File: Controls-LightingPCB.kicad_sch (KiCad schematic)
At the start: 92 parts, among them J1 MinionConn, J10 INTERNAL_RIGHTBLINK, J11 INTERNAL_LEFTBLINK, J12 EXTERNAL_RIGHTBLINK, J13 EXTERNAL_HDLT, J14 EXTERNAL_BRAKELIGHT, J2 12VPWRCONN, J3 CRUZ_ST_INDICATOR_33v, J4 CRUZ_EN_INDICATOR_33v, J5 REGEN_INDICATOR_33v, J6 NEU_INDICATOR_33v, J7 FOR_INDICATOR_33v, J8 REV_INDICATOR_33v, J9 EXTERNAL_LEFTBLINK, Q1 2N7000, Q2 2N7000, Q3 2N7000, Q4 2N7000, Q5 2N7000, SW1 CRUISE_SET, SW2 CRUISE_ENABLE, SW3 F/R_SW, SW4 REGEN_SW, SW5 TURN_SIGNAL_SW, U1 NCP1117-3.3_SOT223

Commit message: Pico-Claps connectors + traces
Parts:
- HZD_SW1, J10, J11, J12, J13, J14, J2, J3, J4, J5, J6, J7, J8, J9, SW1, SW2, SW4: footprint Connector_Molex:Molex_Micro-Fit_3.0_43650-0200_1x02_P3.00mm_Horizontal -> Connector_Molex:Molex_Pico-Clasp_501331-0207_1x02-1MP_P1.00mm_Vertical
- J1: footprint Connector_Molex:Molex_Micro-Fit_3.0_43650-0900_1x09_P3.00mm_Horizontal -> Connector_Molex:Molex_Pico-Clasp_501331-0907_1x09-1MP_P1.00mm_Vertical
- SW3, SW5: footprint Connector_Molex:Molex_Micro-Fit_3.0_43650-0300_1x03_P3.00mm_Horizontal -> Connector_Molex:Molex_Pico-Clasp_501331-0307_1x03-1MP_P1.00mm_Vertical

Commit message: Changed to SMD mosfets
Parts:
- Q1, Q2, Q3, Q4, Q5: footprint Package_TO_SOT_THT:TO-92_Inline -> Package_TO_SOT_SMD:SOT-23
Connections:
- net +3V3 renamed +3.3V
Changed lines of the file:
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@@
     (property "Reference" "Q3" (id 0) (at 237.49 93.98 90))
     (property "Value" "2N7000" (id 1) (at 237.49 96.52 90))
-    (property "Footprint" "Package_TO_SOT_THT:TO-92_Inline" (id 2) (at 235.585 97.79 0)
+    (property "Footprint" "Package_TO_SOT_SMD:SOT-23" (id 2) (at 235.585 97.79 0)
       (effects (font (size 1.27 1.27) italic) (justify left) hide)
     )
-    (property "Datasheet" "https://www.vishay.com/docs/70226/70226.pdf" (id 3) (at 237.49 102.87 0)
+    (property "Datasheet" "https://www.mouser.com/datasheet/2/916/2N7002H-2909812.pdf" (id 3) (at 237.49 102.87 0)
       (effects (font (size 1.27 1.27)) (justify left) hide)
     )
@@
     (property "Reference" "Q5" (id 0) (at 238.76 21.59 90))
     (property "Value" "2N7000" (id 1) (at 238.76 24.13 90))
-    (property "Footprint" "Package_TO_SOT_THT:TO-92_Inline" (id 2) (at 236.855 25.4 0)
+    (property "Footprint" "Package_TO_SOT_SMD:SOT-23" (id 2) (at 236.855 25.4 0)
       (effects (font (size 1.27 1.27) italic) (justify left) hide)
     )
-    (property "Datasheet" "https://www.vishay.com/docs/70226/70226.pdf" (id 3) (at 238.76 30.48 0)
+    (property "Datasheet" "https://www.mouser.com/datasheet/2/916/2N7002H-2909812.pdf" (id 3) (at 238.76 30.48 0)
       (effects (font (size 1.27 1.27)) (justify left) hide)
     )
@@
     (property "Reference" "Q2" (id 0) (at 237.49 69.85 90))
     (property "Value" "2N7000" (id 1) (at 237.49 72.39 90))
-    (property "Footprint" "Package_TO_SOT_THT:TO-92_Inline" (id 2) (at 235.585 73.66 0)
+    (property "Footprint" "Package_TO_SOT_SMD:SOT-23" (id 2) (at 235.585 73.66 0)
       (effects (font (size 1.27 1.27) italic) (justify left) hide)
     )
-    (property "Datasheet" "https://www.vishay.com/docs/70226/70226.pdf" (id 3) (at 237.49 78.74 0)
+    (property "Datasheet" "https://www.mouser.com/datasheet/2/916/2N7002H-2909812.pdf" (id 3) (at 237.49 78.74 0)
       (effects (font (size 1.27 1.27)) (justify left) hide)
     )
@@
     (property "Reference" "Q1" (id 0) (at 237.49 45.72 90))
     (property "Value" "2N7000" (id 1) (at 237.49 48.26 90))
-    (property "Footprint" "Package_TO_SOT_THT:TO-92_Inline" (id 2) (at 235.585 49.53 0)
+    (property "Footprint" "Package_TO_SOT_SMD:SOT-23" (id 2) (at 235.585 49.53 0)
       (effects (font (size 1.27 1.27) italic) (justify left) hide)
     )
-    (property "Datasheet" "https://www.vishay.com/docs/70226/70226.pdf" (id 3) (at 237.49 54.61 0)
+    (property "Datasheet" "https://www.mouser.com/datasheet/2/916/2N7002H-2909812.pdf" (id 3) (at 237.49 54.61 0)
       (effects (font (size 1.27 1.27)) (justify left) hide)
     )
@@
     (property "Reference" "Q4" (id 0) (at 247.015 150.495 0))
     (property "Value" "2N7000" (id 1) (at 247.015 153.035 0))
-    (property "Footprint" "Package_TO_SOT_THT:TO-92_Inline" (id 2) (at 243.205 153.67 0)
+    (property "Footprint" "Package_TO_SOT_SMD:SOT-23" (id 2) (at 243.205 153.67 0)
       (effects (font (size 1.27 1.27) italic) (justify left) hide)
     )
-    (property "Datasheet" "https://www.vishay.com/docs/70226/70226.pdf" (id 3) (at 238.125 151.765 0)
+    (property "Datasheet" "https://www.mouser.com/datasheet/2/916/2N7002H-2909812.pdf" (id 3) (at 238.125 151.765 0)
       (effects (font (size 1.27 1.27)) (justify left) hide)
     )
@@
     )
     (path "/ad0e8c56-9523-4294-a2ce-615be15ed23f"
-      (reference "Q1") (unit 1) (value "2N7000") (footprint "Package_TO_SOT_THT:TO-92_Inline")
+      (reference "Q1") (unit 1) (value "2N7000") (footprint "Package_TO_SOT_SMD:SOT-23")
     )
     (path "/a5dd49cb-a130-4999-9533-e26323d7662d"
-      (reference "Q2") (unit 1) (value "2N7000") (footprint "Package_TO_SOT_THT:TO-92_Inline")
+      (reference "Q2") (unit 1) (value "2N7000") (footprint "Package_TO_SOT_SMD:SOT-23")
     )
     (path "/3198a27d-6bfc-45eb-bfb7-7dcd7e675f29"
-      (reference "Q3") (unit 1) (value "2N7000") (footprint "Package_TO_SOT_THT:TO-92_Inline")
+      (reference "Q3") (unit 1) (value "2N7000") (footprint "Package_TO_SOT_SMD:SOT-23")
     )
     (path "/cf06b1f1-2a1d-4ba2-bbf7-922b9eaa6d79"
-      (reference "Q4") (unit 1) (value "2N7000") (footprint "Package_TO_SOT_THT:TO-92_Inline")
+      (reference "Q4") (unit 1) (value "2N7000") (footprint "Package_TO_SOT_SMD:SOT-23")
     )
     (path "/8c4da0ba-68dc-4ea9-bd3d-de81e85c559f"
-      (reference "Q5") (unit 1) (value "2N7000") (footprint "Package_TO_SOT_THT:TO-92_Inline")
+      (reference "Q5") (unit 1) (value "2N7000") (footprint "Package_TO_SOT_SMD:SOT-23")
     )
     (path "/bf79cd79-9bbf-496d-a03d-63973600490a"

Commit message: First bad layout
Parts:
- HZD_SW1, J10, J11, J12, J13, J14, J2, J3, J4, J5, J6, J7, J8, J9, SW1, SW2, SW4: footprint Connector_Molex:Molex_Pico-Clasp_501331-0207_1x02-1MP_P1.00mm_Vertical -> Connector_Molex:Molex_Micro-Fit_3.0_43650-0215_1x02_P3.00mm_Vertical
- J1: footprint Connector_Molex:Molex_Pico-Clasp_501331-0907_1x09-1MP_P1.00mm_Vertical -> Connector_Molex:Molex_Micro-Fit_3.0_43650-0900_1x09_P3.00mm_Horizontal
- SW3, SW5: footprint Connector_Molex:Molex_Pico-Clasp_501331-0307_1x03-1MP_P1.00mm_Vertical -> Connector_Molex:Molex_Micro-Fit_3.0_43650-0315_1x03_P3.00mm_Vertical

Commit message: finished layout
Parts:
- removed R18, R19: 100k, Resistor_SMD:R_0805_2012Metric, symbol Device:R_Small
- CRUZ EN IND1: renamed from J4
- CRUZ EN SW1: renamed from SW2
- CRUZ SET IND1: renamed from J3
- CRUZ SET SW1: renamed from SW1
- F/R SW1: renamed from SW3; footprint Connector_Molex:Molex_Micro-Fit_3.0_43650-0315_1x03_P3.00mm_Vertical -> Connector_Molex:Molex_Micro-Fit_3.0_43650-0415_1x04_P3.00mm_Vertical
- FORWARD IND1: renamed from J7
- HZD SW1: renamed from HZD_SW1
- L BLINK EXT1: renamed from J9
- L BLINK INT1: renamed from J11
- NEUTRAL IND1: renamed from J6
- R BLINK EXT1: renamed from J12
- R BLINK INT1: renamed from J10
- REGEN IND1: renamed from J5
- REGEN SW1: renamed from SW4
- REV IND1: renamed from J8
- Turn Signal SW1: renamed from SW5
- renumbered TP5 to 12V1, TP3 to 3V3, TP6 to 5V1, J14 to BRAKELIGHT1, TP9 to CLK1, TP2 to GND1, TP1 to GNDPWR1, J13 to HEADLIGHT2, TP8 to Headlight1, TP4 to LeftBlink1, J2 to PWR1, TP7 to RightBlink1

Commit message: component updates
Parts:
- C9: value 10uF -> 33 uF
- R10, R13, R14, R15, R4, R5: value 0k -> 100 Ohm
- R20, R21: value 0k -> 0 Ohm
- R23, R24: value 0 Ohm -> 500 Ohm
- R8: value 6.8k -> 10k
- R9: value 56k -> 10k
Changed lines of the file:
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@@
     (in_bom yes) (on_board yes)
     (property "Reference" "R13" (id 0) (at 172.085 120.015 0))
-    (property "Value" "0k" (id 1) (at 172.085 121.92 0))
+    (property "Value" "100 Ohm" (id 1) (at 173.99 121.92 0))
     (property "Footprint" "Resistor_SMD:R_0805_2012Metric" (id 2) (at 168.91 119.38 0)
       (effects (font (size 1.27 1.27)) hide)
@@
     (in_bom yes) (on_board yes)
     (property "Reference" "R20" (id 0) (at 232.41 120.015 90))
-    (property "Value" "0k" (id 1) (at 232.41 122.555 90))
+    (property "Value" "0 Ohm" (id 1) (at 232.41 122.555 90))
     (property "Footprint" "Resistor_SMD:R_0805_2012Metric" (id 2) (at 230.505 127 0)
       (effects (font (size 1.27 1.27)) hide)
@@
     (in_bom yes) (on_board yes)
     (property "Reference" "R24" (id 0) (at 238.76 86.36 90))
-    (property "Value" "0 Ohm" (id 1) (at 240.03 88.9 90))
+    (property "Value" "500 Ohm" (id 1) (at 240.03 88.9 90))
     (property "Footprint" "Resistor_SMD:R_0805_2012Metric" (id 2) (at 237.49 91.44 0)
       (effects (font (size 1.27 1.27)) hide)
@@
     (in_bom yes) (on_board yes)
     (property "Reference" "R14" (id 0) (at 173.355 132.715 0))
-    (property "Value" "0k" (id 1) (at 173.355 134.62 0))
+    (property "Value" "100 Ohm" (id 1) (at 176.53 134.62 0))
     (property "Footprint" "Resistor_SMD:R_0805_2012Metric" (id 2) (at 170.815 132.715 0)
       (effects (font (size 1.27 1.27)) hide)
@@
       (effects (font (size 1.27 1.27)) (justify right))
     )
-    (property "Value" "56k" (id 1) (at 135.89 55.8799 0)
+    (property "Value" "10k" (id 1) (at 135.89 55.8799 0)
       (effects (font (size 1.27 1.27)) (justify right))
     )
@@
     (in_bom yes) (on_board yes)
     (property "Reference" "R21" (id 0) (at 233.045 137.16 90))
-    (property "Value" "0k" (id 1) (at 233.045 139.7 90))
+    (property "Value" "0 Ohm" (id 1) (at 233.045 139.7 90))
     (property "Footprint" "Resistor_SMD:R_0805_2012Metric" (id 2) (at 231.14 144.145 0)
       (effects (font (size 1.27 1.27)) hide)
@@
       (effects (font (size 1.27 1.27)) (justify left))
     )
-    (property "Value" "6.8k" (id 1) (at 135.89 48.2599 0)
+    (property "Value" "10k" (id 1) (at 135.89 48.2599 0)
       (effects (font (size 1.27 1.27)) (justify left))
     )
@@
     (in_bom yes) (on_board yes)
     (property "Reference" "R15" (id 0) (at 177.165 144.78 0))
-    (property "Value" "0k" (id 1) (at 177.165 146.685 0))
+    (property "Value" "100 Ohm" (id 1) (at 179.07 147.32 0))
     (property "Footprint" "Resistor_SMD:R_0805_2012Metric" (id 2) (at 173.99 144.145 0)
       (effects (font (size 1.27 1.27)) hide)
@@
     (in_bom yes) (on_board yes)
     (property "Reference" "R10" (id 0) (at 139.7 115.57 90))
-    (property "Value" "0k" (id 1) (at 139.7 117.475 90))
+    (property "Value" "100 Ohm" (id 1) (at 140.97 116.84 90))
     (property "Footprint" "Resistor_SMD:R_0805_2012Metric" (id 2) (at 137.795 112.395 0)
       (effects (font (size 1.27 1.27)) hide)
@@
     (in_bom yes) (on_board yes)
     (property "Reference" "R4" (id 0) (at 81.28 117.475 90))
-    (property "Value" "0k" (id 1) (at 81.28 119.38 90))
+    (property "Value" "100 Ohm" (id 1) (at 83.82 119.38 90))
     (property "Footprint" "Resistor_SMD:R_0805_2012Metric" (id 2) (at 79.375 114.3 0)
       (effects (font (size 1.27 1.27)) hide)
@@
       (effects (font (size 1.27 1.27)) (justify left))
     )
-    (property "Value" "10uF" (id 1) (at 127 63.5 0)
+    (property "Value" "33 uF" (id 1) (at 127 63.5 0)
       (effects (font (size 1.27 1.27)) (justify left))
     )
@@
     (in_bom yes) (on_board yes)
     (property "Reference" "R5" (id 0) (at 81.915 156.21 90))
-    (property "Value" "0k" (id 1) (at 81.915 158.115 90))
+    (property "Value" "100 Ohm" (id 1) (at 83.82 158.75 90))
     (property "Footprint" "Resistor_SMD:R_0805_2012Metric" (id 2) (at 80.01 153.035 0)
       (effects (font (size 1.27 1.27)) hide)
@@
     (in_bom yes) (on_board yes)
     (property "Reference" "R23" (id 0) (at 238.76 62.23 90))
-    (property "Value" "0 Ohm" (id 1) (at 240.03 64.77 90))
+    (property "Value" "500 Ohm" (id 1) (at 240.03 64.77 90))
     (property "Footprint" "Resistor_SMD:R_0805_2012Metric" (id 2) (at 237.49 67.31 0)
       (effects (font (size 1.27 1.27)) hide)
@@
     )
     (path "/b3a55782-cbfa-4ad7-a3bc-1a21e5b9d7e1"
-      (reference "C9") (unit 1) (value "10uF") (footprint "Capacitor_SMD:C_0805_2012Metric")
+      (reference "C9") (unit 1) (value "33 uF") (footprint "Capacitor_SMD:C_0805_2012Metric")
     )
     (path "/03b27535-447c-483c-8e98-454a6a39168a"
@@
     )
     (path "/9c10fc17-ccfe-4e69-aa86-c672041d3ca2"
-      (reference "R4") (unit 1) (value "0k") (footprint "Resistor_SMD:R_0805_2012Metric")
+      (reference "R4") (unit 1) (value "100 Ohm") (footprint "Resistor_SMD:R_0805_2012Metric")
     )
     (path "/bf67ec5a-fdc9-4655-ae9a-dfe5faf72199"
-      (reference "R5") (unit 1) (value "0k") (footprint "Resistor_SMD:R_0805_2012Metric")
+      (reference "R5") (unit 1) (value "100 Ohm") (footprint "Resistor_SMD:R_0805_2012Metric")
     )
     (path "/0b46dd1c-57a4-4d34-a081-aa58b25354f8"
@@
     )
     (path "/579a53c9-ab3c-4032-a13e-83c57f96dbc9"
-      (reference "R8") (unit 1) (value "6.8k") (footprint "Resistor_SMD:R_0805_2012Metric")
+      (reference "R8") (unit 1) (value "10k") (footprint "Resistor_SMD:R_0805_2012Metric")
     )
     (path "/35b071f2-161c-49bc-b89a-f680527e0dea"
-      (reference "R9") (unit 1) (value "56k") (footprint "Resistor_SMD:R_0805_2012Metric")
+      (reference "R9") (unit 1) (value "10k") (footprint "Resistor_SMD:R_0805_2012Metric")
     )
     (path "/943566fc-e0ec-4811-a35c-3b8867aae60d"
-      (reference "R10") (unit 1) (value "0k") (footprint "Resistor_SMD:R_0805_2012Metric")
+      (reference "R10") (unit 1) (value "100 Ohm") (footprint "Resistor_SMD:R_0805_2012Metric")
     )
     (path "/421bd5df-1649-4123-ab2b-fa7f213c86e8"
@@
     )
     (path "/08e7c18d-e700-4c5b-ae98-5a65f509b387"
-      (reference "R13") (unit 1) (value "0k") (footprint "Resistor_SMD:R_0805_2012Metric")
+      (reference "R13") (unit 1) (value "100 Ohm") (footprint "Resistor_SMD:R_0805_2012Metric")
     )
     (path "/289f6036-ef79-4e79-8863-68c618e8eafc"
-      (reference "R14") (unit 1) (value "0k") (footprint "Resistor_SMD:R_0805_2012Metric")
+      (reference "R14") (unit 1) (value "100 Ohm") (footprint "Resistor_SMD:R_0805_2012Metric")
     )
     (path "/610c1617-a221-4760-8695-07d2d71b427f"
-      (reference "R15") (unit 1) (value "0k") (footprint "Resistor_SMD:R_0805_2012Metric")
+      (reference "R15") (unit 1) (value "100 Ohm") (footprint "Resistor_SMD:R_0805_2012Metric")
     )
     (path "/5884bc66-6373-4b10-8c5d-8d80d29d8235"
@@
     )
     (path "/0f8225d3-8219-489b-b209-40bdef973e35"
-      (reference "R20") (unit 1) (value "0k") (footprint "Resistor_SMD:R_0805_2012Metric")
+      (reference "R20") (unit 1) (value "0 Ohm") (footprint "Resistor_SMD:R_0805_2012Metric")
     )
     (path "/37ed7774-c67f-4bb7-ba89-37762335d011"
-      (reference "R21") (unit 1) (value "0k") (footprint "Resistor_SMD:R_0805_2012Metric")
+      (reference "R21") (unit 1) (value "0 Ohm") (footprint "Resistor_SMD:R_0805_2012Metric")
     )
     (path "/946bde52-dc85-4916-a3c3-bde85e985d1b"
@@
     )
     (path "/fb9184e4-384d-4f42-b022-6d4808c8e4a7"
-      (reference "R23") (unit 1) (value "0 Ohm") (footprint "Resistor_SMD:R_0805_2012Metric")
+      (reference "R23") (unit 1) (value "500 Ohm") (footprint "Resistor_SMD:R_0805_2012Metric")
     )
     (path "/1507a5d3-239c-4d3f-8651-9813e63d0b2c"
-      (reference "R24") (unit 1) (value "0 Ohm") (footprint "Resistor_SMD:R_0805_2012Metric")
+      (reference "R24") (unit 1) (value "500 Ohm") (footprint "Resistor_SMD:R_0805_2012Metric")
     )
     (path "/eaf3525f-dc49-455e-8131-3078130e9ef1"

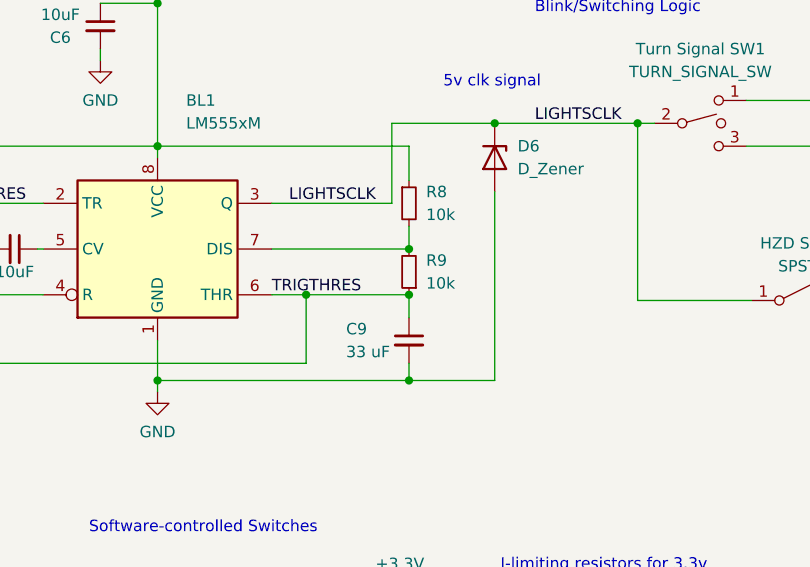
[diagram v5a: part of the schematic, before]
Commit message: fixed timer
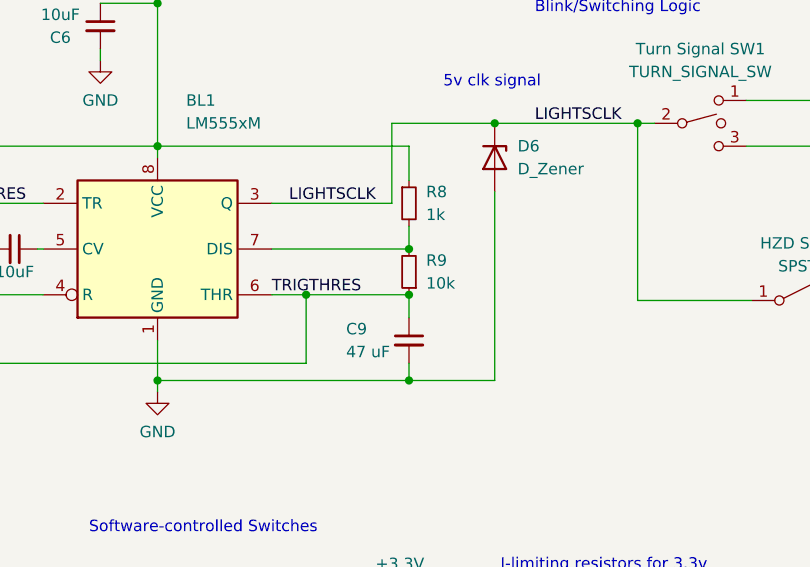
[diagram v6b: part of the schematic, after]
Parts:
- C9: value 33 uF -> 47 uF
- R8: value 10k -> 1k
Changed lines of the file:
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@@
       (effects (font (size 1.27 1.27)) (justify left))
     )
-    (property "Value" "10k" (id 1) (at 135.89 48.2599 0)
+    (property "Value" "1k" (id 1) (at 135.89 48.2599 0)
       (effects (font (size 1.27 1.27)) (justify left))
     )
@@
       (effects (font (size 1.27 1.27)) (justify left))
     )
-    (property "Value" "33 uF" (id 1) (at 127 63.5 0)
+    (property "Value" "47 uF" (id 1) (at 127 63.5 0)
       (effects (font (size 1.27 1.27)) (justify left))
     )
@@
     )
     (path "/b3a55782-cbfa-4ad7-a3bc-1a21e5b9d7e1"
-      (reference "C9") (unit 1) (value "33 uF") (footprint "Capacitor_SMD:C_0805_2012Metric")
+      (reference "C9") (unit 1) (value "47 uF") (footprint "Capacitor_SMD:C_0805_2012Metric")
     )
     (path "/03b27535-447c-483c-8e98-454a6a39168a"
@@
     )
     (path "/579a53c9-ab3c-4032-a13e-83c57f96dbc9"
-      (reference "R8") (unit 1) (value "10k") (footprint "Resistor_SMD:R_0805_2012Metric")
+      (reference "R8") (unit 1) (value "1k") (footprint "Resistor_SMD:R_0805_2012Metric")
     )
     (path "/35b071f2-161c-49bc-b89a-f680527e0dea"

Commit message: Change schematics
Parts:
- removed C12: C_Small, Capacitor_SMD:C_0805_2012Metric, symbol Device:C_Small
- removed D4: 1N5400, Diode_THT:D_DO-201AD_P15.24mm_Horizontal, symbol Diode:1N5400
- removed REGEN SW1: REGEN_SW, Connector_Molex:Molex_Micro-Fit_3.0_43650-0215_1x02_P3.00mm_Vertical, symbol Switch:SW_SPST
- added REGENSW1: REGEN, Connector_Molex:Molex_Micro-Fit_3.0_43650-0215_1x02_P3.00mm_Vertical, symbol Switch:SW_Push
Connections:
- net +3.3V: now also REGENSW1.1
- net GND: now also FORWARD IND1.2 (Pin_2), NEUTRAL IND1.2 (Pin_2), REV IND1.2 (Pin_2); no longer FORWARD IND1.1 (Pin_1), NEUTRAL IND1.1 (Pin_1), REV IND1.1 (Pin_1)
- net REGEN_SW: now also REGENSW1.2
- net at J1.8 (Pin_8): now also D5.2 (A2), FB3.1
- net at R13.1: now also NEUTRAL IND1.1 (Pin_1); no longer NEUTRAL IND1.2 (Pin_2)
- net NEU_SW: now reaches C8.2, F/R SW1.2, R13.2, R6.2
- net at R14.1: now also FORWARD IND1.1 (Pin_1); no longer FORWARD IND1.2 (Pin_2)
- net at R15.1: now also REV IND1.1 (Pin_1); no longer REV IND1.2 (Pin_2)
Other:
- moved on the sheet: F/R SW1, FORWARD IND1, NEUTRAL IND1, R15, REV IND1
